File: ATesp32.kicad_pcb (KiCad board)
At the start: 4 copper layers, 18 x 51.2 mm, 51 parts, among them J1 USB_C_Receptacle_USB2.0_16P, J2 JST PH, Q1 DMP2045U, SW1 RESET, SW2 BOOT, U1 ESP32-S3, U2 ATmega32A-P, U3 MCP73831-2-OT, U4 AP2112K-3.3, U5 CP2102N-Axx-xQFN24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

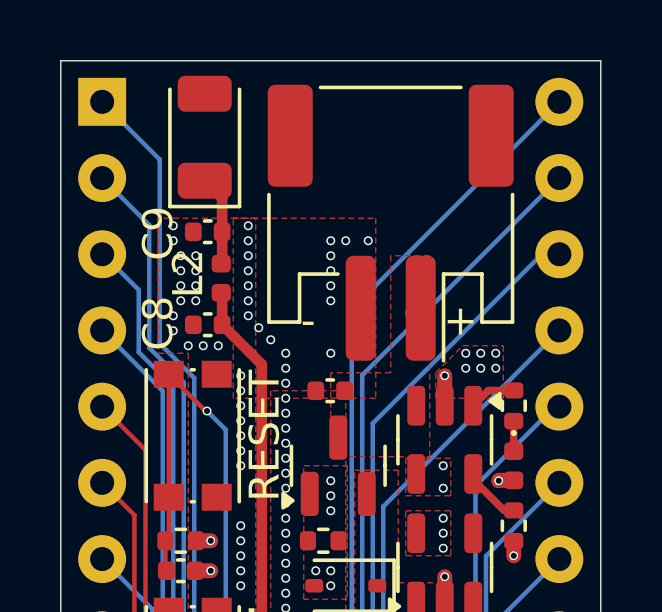
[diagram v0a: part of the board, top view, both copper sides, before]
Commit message: fix bug - correct use of open drain status signal of lipo charger
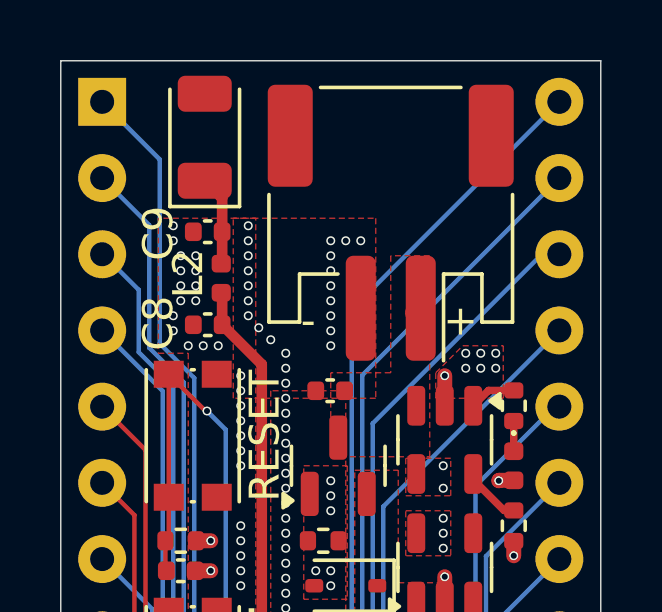
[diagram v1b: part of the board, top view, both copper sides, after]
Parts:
- U3: value MCP73831-2-OT -> MCP73832
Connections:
- D2 pad 2: GND -> +5V
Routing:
- net +5V: track 0.00 -> 0.51 mm, vias 17 -> 18
- net GND: track 11.4 -> 10.9 mm, vias 113 -> 114
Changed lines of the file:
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@@
 			)
 		)
-		(property "Value" "MCP73831-2-OT"
+		(property "Value" "MCP73832"
 			(at 0 2.4 90)
 			(layer "F.Fab")
@@
 			(layers "F.Cu" "F.Paste" "F.Mask")
 			(roundrect_rratio 0.25)
-			(net 3 "GND")
+			(net 6 "+5V")
 			(pinfunction "A")
 			(pintype "passive")
@@
 	)
 	(segment
-		(start 90.1 63.985)
-		(end 89.615 63.985)
-		(width 0.5)
-		(layer "F.Cu")
-		(net 3)
-	)
-	(segment
 		(start 87.8 61.5)
 		(end 87.8 60.5)
@@
 	)
 	(segment
-		(start 89.615 63.985)
-		(end 89.6 64)
-		(width 0.5)
-		(layer "F.Cu")
-		(net 3)
-	)
-	(segment
 		(start 83.25 92.732108)
 		(end 83.259699 92.741807)
@@
 	)
 	(via
+		(at 84 58.5)
+		(size 0.3)
+		(drill 0.2)
+		(layers "F.Cu" "B.Cu")
+		(free yes)
+		(net 3)
+	)
+	(via
 		(at 87.5 87.85)
 		(size 0.3)
@@
 	)
 	(via
-		(at 84 59.75)
+		(at 84 59.5)
 		(size 0.3)
 		(drill 0.2)
@@
 	)
 	(via
+		(at 84 59)
+		(size 0.3)
+		(drill 0.2)
+		(layers "F.Cu" "B.Cu")
+		(free yes)
+		(net 3)
+	)
+	(via
 		(at 81.25 58.5)
 		(size 0.3)
@@
 	)
 	(via
-		(at 89.6 64)
-		(size 0.3)
-		(drill 0.2)
-		(layers "F.Cu" "B.Cu")
-		(net 3)
-	)
-	(via
 		(at 82.5 66.75)
 		(size 0.3)
@@
 	)
 	(via
-		(at 85.25 56)
+		(at 85 56)
 		(size 0.3)
 		(drill 0.2)
@@
 		(net 5)
 	)
+	(segment
+		(start 90.1 63.985)
+		(end 89.615 63.985)
+		(width 0.5)
+		(layer "F.Cu")
+		(net 6)
+	)
+	(segment
+		(start 89.615 63.985)
+		(end 89.6 64)
+		(width 0.5)
+		(layer "F.Cu")
+		(net 6)
+	)
 	(via
 		(at 84 67)
@@
 		(net 6)
 	)
+	(via
+		(at 89.6 64)
+		(size 0.3)
+		(drill 0.2)
+		(layers "F.Cu" "B.Cu")
+		(net 6)
+	)

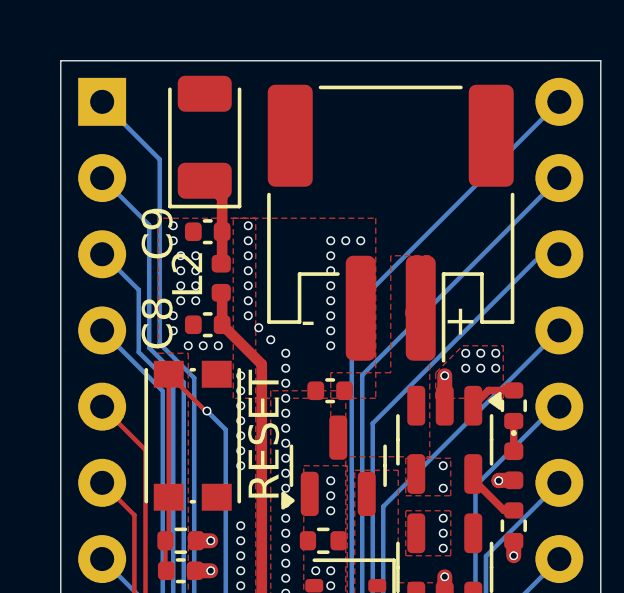
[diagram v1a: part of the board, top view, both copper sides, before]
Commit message: spec components for JLC
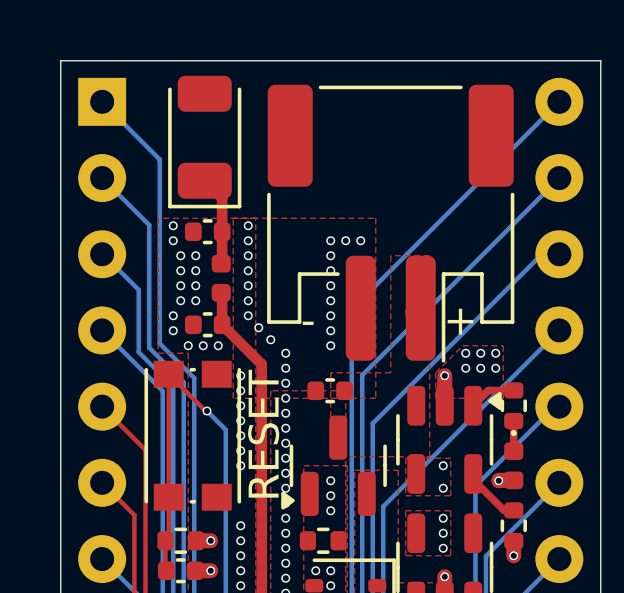
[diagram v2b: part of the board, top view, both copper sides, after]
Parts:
- R14, R15, R6: value 10K -> 5.1K
- U2: value ATmega32A-P -> HEADER

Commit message: Generate production files. More clear part names for ESP and LiPo charger
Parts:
- U1: value ESP32-S3 -> ESP32-S3FH4R2
- U3: value MCP73832 -> MCP73832-2
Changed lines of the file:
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@@
 			(viasonmask no)
 			(mode 1)
-			(useauxorigin no)
+			(useauxorigin yes)
 			(hpglpennumber 1)
 			(hpglpenspeed 20)
@@
 			(outputformat 1)
 			(mirror no)
-			(drillshape 1)
+			(drillshape 0)
 			(scaleselection 1)
-			(outputdirectory "")
+			(outputdirectory "Fabrication/")
 		)
 	)
@@
 			)
 		)
-		(property "Value" "MCP73832"
+		(property "Value" "MCP73832-2"
 			(at 0 2.4 90)
 			(layer "F.Fab")
@@
 		(sheetname "Root")
 		(sheetfile "ATesp32.kicad_sch")
-		(attr through_hole exclude_from_pos_files allow_missing_courtyard)
+		(attr through_hole exclude_from_pos_files exclude_from_bom allow_missing_courtyard
+			dnp
+		)
 		(fp_line
 			(start 0.255 -0.27)
@@
 			)
 		)
-		(property "Value" "ESP32-S3"
+		(property "Value" "ESP32-S3FH4R2"
 			(at 0 4.800001 135)
 			(layer "F.Fab")
@@
 		(tags "capacitor")
 		(property "Reference" "C8"
-			(at 1.65 0.05 270)
+			(at 1.65 0.05 -90)
 			(layer "F.SilkS")
 			(hide yes)
@@
 		(sheetfile "ATesp32.kicad_sch")
 		(zone_connect 1)
-		(attr exclude_from_pos_files exclude_from_bom)
+		(attr exclude_from_pos_files exclude_from_bom dnp)
 		(fp_line
 			(start -0.7 -1)
@@
 		(sheetfile "ATesp32.kicad_sch")
 		(zone_connect 1)
-		(attr exclude_from_pos_files exclude_from_bom)
+		(attr exclude_from_pos_files exclude_from_bom dnp)
 		(fp_line
 			(start 1.4 -0.3)
@@
 		(sheetfile "ATesp32_USB.kicad_sch")
 		(zone_connect 1)
-		(attr exclude_from_pos_files exclude_from_bom)
+		(attr exclude_from_pos_files exclude_from_bom dnp)
 		(net_tie_pad_groups "1, 2")
 		(fp_poly
@@
 		(sheetfile "ATesp32_USB.kicad_sch")
 		(zone_connect 1)
-		(attr exclude_from_pos_files exclude_from_bom)
+		(attr exclude_from_pos_files exclude_from_bom dnp)
 		(net_tie_pad_groups "1, 2")
 		(fp_poly

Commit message: Add some Mouser PNs
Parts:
- J1: footprint Connector_USB:USB_C_Receptacle_G-Switch_GT-USB-7010ASV -> Connector_USB:USB_C_Receptacle_GCT_USB4105-xx-A_16P_TopMnt_Horizontal

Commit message: update manf outputs
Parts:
- U3: value MCP73832-2 -> MCP73832T-2
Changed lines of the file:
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@@
 			)
 		)
-		(property "Mouser" "187-CL05B104KO5NNNC"
+		(property "Mouser" ""
 			(at 0 0 45)
 			(unlocked yes)
@@
 			)
 		)
-		(property "Mouser" "187-CL05B104KO5NNNC"
+		(property "Mouser" ""
 			(at 0 0 -135)
 			(unlocked yes)
@@
 			)
 		)
+		(property "DigiKey" "AP2112K-3.3TRG1DICT-ND"
+			(at 0 0 90)
+			(unlocked yes)
+			(layer "F.Fab")
+			(hide yes)
+			(effects
+				(font
+					(size 1 1)
+					(thickness 0.15)
+				)
+			)
+		)
 		(property ki_fp_filters "SOT?23?5*")
 		(sheetname "POWER")
@@
 			)
 		)
-		(property "Value" "MCP73832-2"
+		(property "Value" "MCP73832T-2"
 			(at 0 2.4 90)
 			(layer "F.Fab")
@@
 			)
 		)
+		(property "DigiKey" "MCP73832T-2ACI/OTCT-ND"
+			(at 0 0 -90)
+			(unlocked yes)
+			(layer "F.Fab")
+			(hide yes)
+			(effects
+				(font
+					(size 1 1)
+					(thickness 0.15)
+				)
+			)
+		)
 		(property ki_fp_filters "SOT?23*")
 		(sheetname "POWER")
@@
 			)
 		)
-		(property "Mouser" "187-CL05B104KO5NNNC"
+		(property "Mouser" ""
 			(at 0 0 135)
 			(unlocked yes)
@@
 			)
 		)
+		(property "DigiKey" "336-5887-ND"
+			(at 0 0 90)
+			(unlocked yes)
+			(layer "F.Fab")
+			(hide yes)
+			(effects
+				(font
+					(size 1 1)
+					(thickness 0.15)
+				)
+			)
+		)
 		(property ki_fp_filters "QFN*4x4mm*P0.5mm*")
 		(sheetname "USB")
@@
 			)
 		)
-		(property "Mouser" "187-CL05B104KO5NNNC"
+		(property "Mouser" ""
 			(at 0 0 0)
 			(unlocked yes)
@@
 			)
 		)
-		(property "Mouser" "187-CL05B104KO5NNNC"
+		(property "Mouser" ""
 			(at 0 0 -135)
 			(unlocked yes)
@@
 			)
 		)
-		(property "Mouser" "187-CL05B104KO5NNNC"
+		(property "Mouser" ""
 			(at 0 0 -90)
 			(unlocked yes)

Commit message: USB-UART Bridge LEDs had wrong orientation. Fixed
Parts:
- turned D5 to 180 degrees
- turned D6 to 180 degrees
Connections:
- D5 pad 1: Net-(D5-K) -> GND
- D5 pad 2: GND -> Net-(D5-A)
- D6 pad 1: Net-(D6-K) -> GND
- D6 pad 2: GND -> Net-(D6-A)
- R14 pad 2: Net-(D5-K) -> Net-(D5-A)
- R15 pad 2: Net-(D6-K) -> Net-(D6-A)
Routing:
- net Net-(D5-K): track 1.51 -> 0.00 mm
- net Net-(D5-A): track 0.00 -> 1.51 mm
- net Net-(D6-K): track 1.01 -> 0.00 mm
- net Net-(D6-A): track 0.00 -> 1.01 mm
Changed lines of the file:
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@@
 	(net 11 "Net-(U5-VDD)")
 	(net 12 "Net-(D2-K)")
-	(net 13 "Net-(D5-K)")
-	(net 14 "Net-(D6-K)")
+	(net 13 "Net-(D5-A)")
+	(net 14 "Net-(D6-A)")
 	(net 15 "Net-(J1-CC2)")
 	(net 16 "D-")
@@
 			(layers "F.Cu" "F.Paste" "F.Mask")
 			(roundrect_rratio 0.25)
-			(net 13 "Net-(D5-K)")
+			(net 13 "Net-(D5-A)")
 			(pintype "passive")
 		)
@@
 	(footprint "LED_SMD:LED_0402_1005Metric"
 		(layer "F.Cu")
-		(at 87.9 87)
+		(at 87.9 87 180)
 		(descr "LED SMD 0402 (1005 Metric), square (rectangular) end terminal, IPC_7351 nominal, (Body size source: http://www.tortai-tech.com/upload/download/2011102023233369053.pdf), generated with kicad-footprint-generator")
 		(tags "LED")
 		(property "Reference" "D6"
-			(at 0 -1.17 0)
+			(at 0 -1.17 360)
 			(layer "F.SilkS")
 			(hide yes)
@@
 		)
 		(property "Value" "LED_Small"
-			(at 0 1.17 0)
+			(at 0 1.17 360)
 			(layer "F.Fab")
 			(effects
@@
 		)
 		(property "Footprint" "LED_SMD:LED_0402_1005Metric"
-			(at 0 0 0)
+			(at 0 0 180)
 			(unlocked yes)
 			(layer "F.Fab")
@@
 		)
 		(property "Datasheet" ""
-			(at 0 0 0)
+			(at 0 0 180)
 			(unlocked yes)
 			(layer "F.Fab")
@@
 		)
 		(property "Description" "Light emitting diode, small symbol"
-			(at 0 0 0)
+			(at 0 0 180)
 			(unlocked yes)
 			(layer "F.Fab")
@@
 		)
 		(property "Sim.Device" ""
-			(at 0 0 0)
+			(at 0 0 180)
 			(unlocked yes)
 			(layer "F.Fab")
@@
 		)
 		(property "Sim.Pins" ""
-			(at 0 0 0)
+			(at 0 0 180)
 			(unlocked yes)
 			(layer "F.Fab")
@@
 		)
 		(property "Sim.Type" ""
-			(at 0 0 0)
+			(at 0 0 180)
 			(unlocked yes)
 			(layer "F.Fab")
@@
 		)
 		(property "LCSC" "C510300"
-			(at 0 0 0)
+			(at 0 0 180)
 			(unlocked yes)
 			(layer "F.Fab")
@@
 		)
 		(property "DigiKey" "SML-P11UTT86RCT-ND"
-			(at 0 0 0)
+			(at 0 0 180)
 			(unlocked yes)
 			(layer "F.Fab")
@@
 		)
 		(fp_line
-			(start -0.93 -0.47)
-			(end 0.93 -0.47)
+			(start 0.93 0.47)
+			(end -0.93 0.47)
 			(stroke
 				(width 0.05)
@@
 		)
 		(fp_line
-			(start -0.93 0.47)
-			(end -0.93 -0.47)
+			(start 0.93 -0.47)
+			(end 0.93 0.47)
 			(stroke
 				(width 0.05)
@@
 		)
 		(fp_line
-			(start 0.93 -0.47)
-			(end 0.93 0.47)
+			(start -0.93 0.47)
+			(end -0.93 -0.47)
 			(stroke
 				(width 0.05)
@@
 		)
 		(fp_line
-			(start 0.93 0.47)
-			(end -0.93 0.47)
+			(start -0.93 -0.47)
+			(end 0.93 -0.47)
 			(stroke
 				(width 0.05)
@@
 		)
 		(fp_line
-			(start -0.5 -0.25)
-			(end 0.5 -0.25)
+			(start 0.5 0.25)
+			(end -0.5 0.25)
 			(stroke
 				(width 0.1)
@@
 		)
 		(fp_line
-			(start -0.5 0.25)
-			(end -0.5 -0.25)
+			(start 0.5 -0.25)
+			(end 0.5 0.25)
 			(stroke
 				(width 0.1)
@@
 		)
 		(fp_line
-			(start -0.4 0.25)
-			(end -0.4 -0.25)
+			(start -0.3 0.25)
+			(end -0.3 -0.25)
 			(stroke
 				(width 0.1)
@@
 		)
 		(fp_line
-			(start -0.3 0.25)
-			(end -0.3 -0.25)
+			(start -0.4 0.25)
+			(end -0.4 -0.25)
 			(stroke
 				(width 0.1)
@@
 		)
 		(fp_line
-			(start 0.5 -0.25)
-			(end 0.5 0.25)
+			(start -0.5 0.25)
+			(end -0.5 -0.25)
 			(stroke
 				(width 0.1)
@@
 		)
 		(fp_line
-			(start 0.5 0.25)
-			(end -0.5 0.25)
+			(start -0.5 -0.25)
+			(end 0.5 -0.25)
 			(stroke
 				(width 0.1)
@@
 		)
 		(fp_text user "${REFERENCE}"
-			(at 0 0 0)
+			(at 0 0 360)
 			(layer "F.Fab")
 			(effects
@@
 		)
 		(pad "1" smd roundrect
-			(at -0.485 0)
+			(at -0.485 0 180)
 			(size 0.59 0.64)
 			(layers "F.Cu" "F.Paste" "F.Mask")
 			(roundrect_rratio 0.25)
-			(net 14 "Net-(D6-K)")
+			(net 3 "GND")
 			(pinfunction "K")
 			(pintype "passive")
 		)
 		(pad "2" smd roundrect
-			(at 0.485 0)
+			(at 0.485 0 180)
 			(size 0.59 0.64)
 			(layers "F.Cu" "F.Paste" "F.Mask")
 			(roundrect_rratio 0.25)
-			(net 3 "GND")
+			(net 14 "Net-(D6-A)")
 			(pinfunction "A")
 			(pintype "passive")
@@
 	(footprint "LED_SMD:LED_0402_1005Metric"
 		(layer "F.Cu")
-		(at 87.9 86)
+		(at 87.9 86 180)
 		(descr "LED SMD 0402 (1005 Metric), square (rectangular) end terminal, IPC_7351 nominal, (Body size source: http://www.tortai-tech.com/upload/download/2011102023233369053.pdf), generated with kicad-footprint-generator")
 		(tags "LED")
 		(property "Reference" "D5"
-			(at 0 -1.17 0)
+			(at 0 -1.17 360)
 			(layer "F.SilkS")
 			(hide yes)
@@
 		)
 		(property "Value" "LED_Small"
-			(at 0 1.17 0)
+			(at 0 1.17 360)
 			(layer "F.Fab")
 			(effects
@@
 		)
 		(property "Footprint" "LED_SMD:LED_0402_1005Metric"
-			(at 0 0 0)
+			(at 0 0 180)
 			(unlocked yes)
 			(layer "F.Fab")
@@
 		)
 		(property "Datasheet" ""
-			(at 0 0 0)
+			(at 0 0 180)
 			(unlocked yes)
 			(layer "F.Fab")
@@
 		)
 		(property "Description" "Light emitting diode, small symbol"
-			(at 0 0 0)
+			(at 0 0 180)
 			(unlocked yes)
 			(layer "F.Fab")
@@
 		)
 		(property "Sim.Device" ""
-			(at 0 0 0)
+			(at 0 0 180)
 			(unlocked yes)
 			(layer "F.Fab")
@@
 		)
 		(property "Sim.Pins" ""
-			(at 0 0 0)
+			(at 0 0 180)
 			(unlocked yes)
 			(layer "F.Fab")
@@
 		)
 		(property "Sim.Type" ""
-			(at 0 0 0)
+			(at 0 0 180)
 			(unlocked yes)
 			(layer "F.Fab")
@@
 		)
 		(property "LCSC" "C510300"
-			(at 0 0 0)
+			(at 0 0 180)
 			(unlocked yes)
 			(layer "F.Fab")
@@
 		)
 		(property "DigiKey" "SML-P11UTT86RCT-ND"
-			(at 0 0 0)
+			(at 0 0 180)
 			(unlocked yes)
 			(layer "F.Fab")
@@
 		)
 		(fp_line
-			(start -0.93 -0.47)
-			(end 0.93 -0.47)
+			(start 0.93 0.47)
+			(end -0.93 0.47)
 			(stroke
 				(width 0.05)
@@
 		)
 		(fp_line
-			(start -0.93 0.47)
-			(end -0.93 -0.47)
+			(start 0.93 -0.47)
+			(end 0.93 0.47)
 			(stroke
 				(width 0.05)
@@
 		)
 		(fp_line
-			(start 0.93 -0.47)
-			(end 0.93 0.47)
+			(start -0.93 0.47)
+			(end -0.93 -0.47)
 			(stroke
 				(width 0.05)
@@
 		)
 		(fp_line
-			(start 0.93 0.47)
-			(end -0.93 0.47)
+			(start -0.93 -0.47)
+			(end 0.93 -0.47)
 			(stroke
 				(width 0.05)
@@
 		)
 		(fp_line
-			(start -0.5 -0.25)
-			(end 0.5 -0.25)
+			(start 0.5 0.25)
+			(end -0.5 0.25)
 			(stroke
 				(width 0.1)
@@
 		)
 		(fp_line
-			(start -0.5 0.25)
-			(end -0.5 -0.25)
+			(start 0.5 -0.25)
+			(end 0.5 0.25)
 			(stroke
 				(width 0.1)
@@
 		)
 		(fp_line
-			(start -0.4 0.25)
-			(end -0.4 -0.25)
+			(start -0.3 0.25)
+			(end -0.3 -0.25)
 			(stroke
 				(width 0.1)
@@
 		)
 		(fp_line
-			(start -0.3 0.25)
-			(end -0.3 -0.25)
+			(start -0.4 0.25)
+			(end -0.4 -0.25)
 			(stroke
 				(width 0.1)
@@
 		)
 		(fp_line
-			(start 0.5 -0.25)
-			(end 0.5 0.25)
+			(start -0.5 0.25)
+			(end -0.5 -0.25)
 			(stroke
 				(width 0.1)
@@
 		)
 		(fp_line
-			(start 0.5 0.25)
-			(end -0.5 0.25)
+			(start -0.5 -0.25)
+			(end 0.5 -0.25)
 			(stroke
 				(width 0.1)
@@
 		)
 		(fp_text user "${REFERENCE}"
-			(at 0 0 0)
+			(at 0 0 360)
 			(layer "F.Fab")
 			(effects
@@
 		)
 		(pad "1" smd roundrect
-			(at -0.485 0)
+			(at -0.485 0 180)
 			(size 0.59 0.64)
 			(layers "F.Cu" "F.Paste" "F.Mask")
 			(roundrect_rratio 0.25)
-			(net 13 "Net-(D5-K)")
+			(net 3 "GND")
 			(pinfunction "K")
 			(pintype "passive")
 		)
 		(pad "2" smd roundrect
-			(at 0.485 0)
+			(at 0.485 0 180)
 			(size 0.59 0.64)
 			(layers "F.Cu" "F.Paste" "F.Mask")
 			(roundrect_rratio 0.25)
-			(net 3 "GND")
+			(net 13 "Net-(D5-A)")
 			(pinfunction "A")
 			(pintype "passive")
@@
 			(layers "F.Cu" "F.Paste" "F.Mask")
 			(roundrect_rratio 0.25)
-			(net 14 "Net-(D6-K)")
+			(net 14 "Net-(D6-A)")
 			(pintype "passive")
 		)
@@
 		(polygon
 			(pts
-				(xy 88 85.65) (xy 88.85 85.65) (xy 88.85 88.55) (xy 88 88.55) (xy 88 88.1) (xy 86.7 88.1) (xy 86.7 87.5)
+				(xy 87.95 85.65) (xy 88.85 85.65) (xy 88.85 88.55) (xy 88 88.55) (xy 88 88.1) (xy 86.7 88.1) (xy 86.7 87.5)
 				(xy 87.95 87.5)
 			)

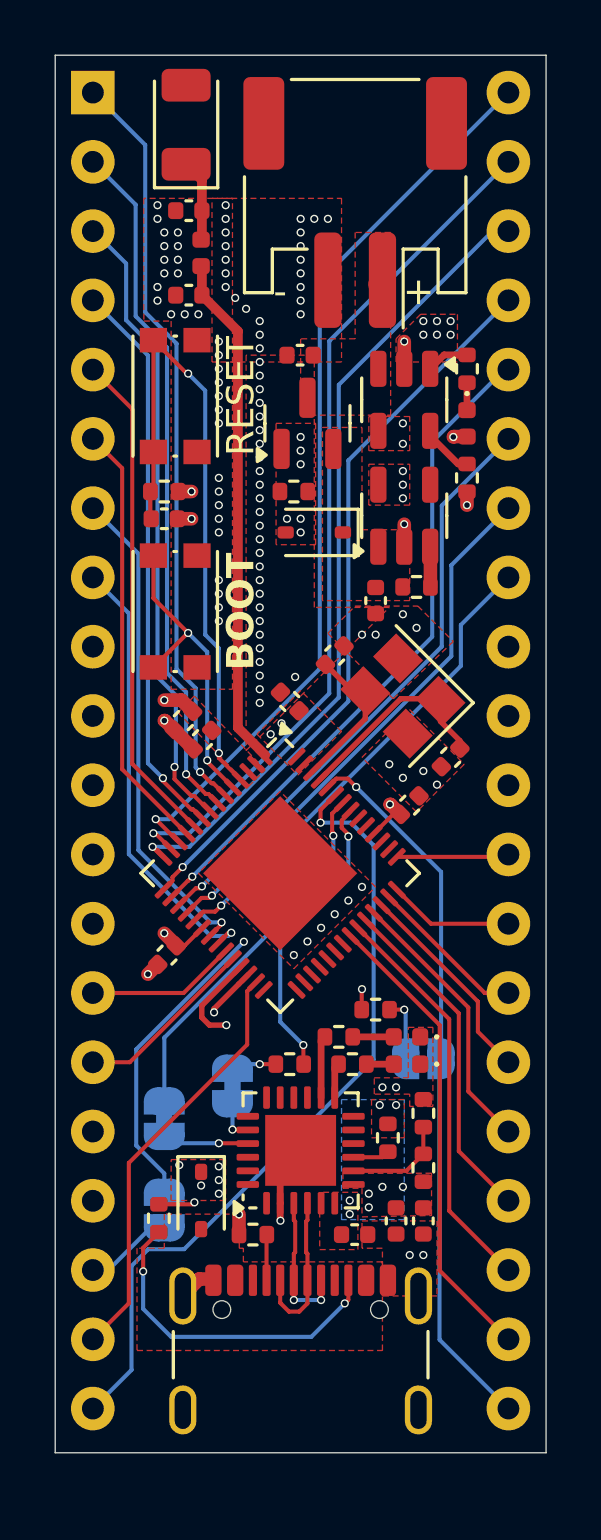
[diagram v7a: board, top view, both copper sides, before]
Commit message: LEDs were persistently on. Change to active low config see CP2102N datasheet fig 4.3
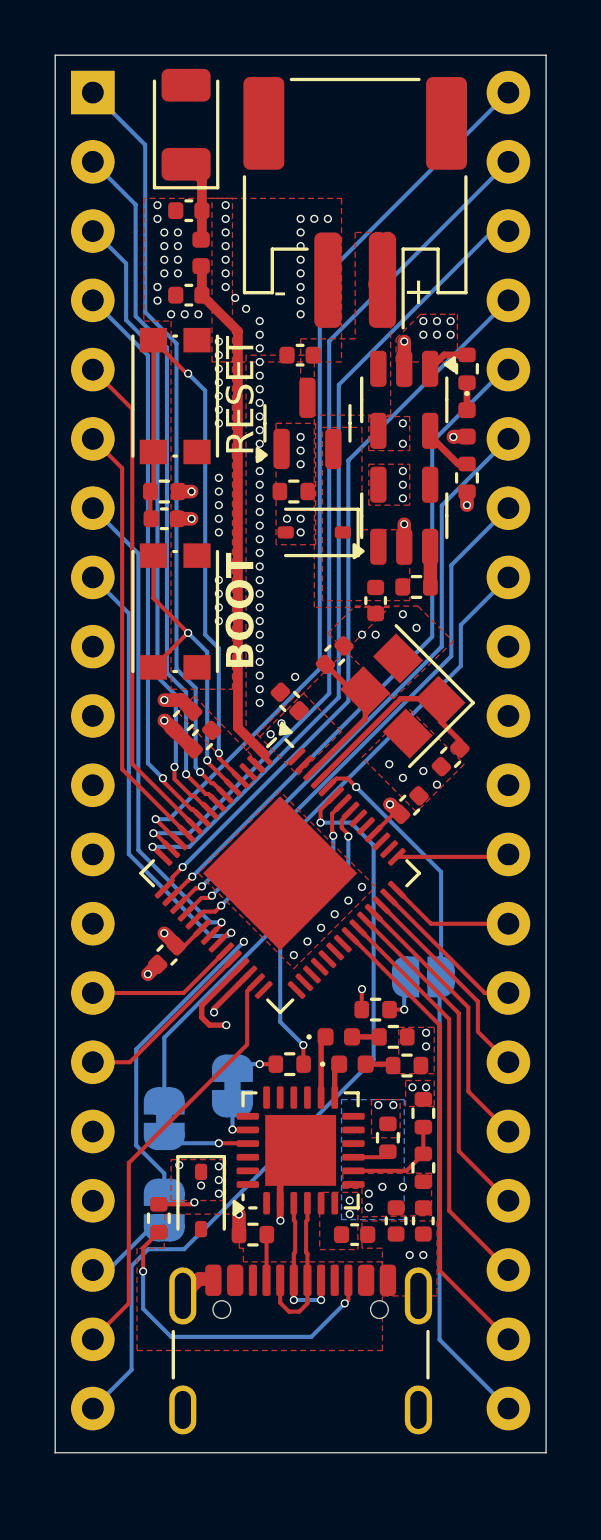
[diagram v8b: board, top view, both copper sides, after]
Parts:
- moved JP6 3.00 mm to (88.5, 83.8)
- moved D5 2.50 mm to (85.4, 86.0), turned to 0 degrees
- moved R15 2.00 mm to (87.9, 87.0)
- moved D6 2.00 mm to (85.9, 87.0), turned to 0 degrees
- moved R14 2.00 mm to (87.4, 86.0)
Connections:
- D5 pad 1: GND -> Net-(D5-K)
- D6 pad 1: GND -> Net-(D6-K)
- R14 pad 1: Net-(U5-~{TXT}/GPIO.0) -> Net-(D5-A)
- R14 pad 2: Net-(D5-A) -> +5V
- R15 pad 1: Net-(U5-~{RXT}/GPIO.1) -> Net-(D6-A)
- R15 pad 2: Net-(D6-A) -> +5V
- U5 pad 13: Net-(U5-~{RXT}/GPIO.1) -> Net-(D6-K)
- U5 pad 14: Net-(U5-~{TXT}/GPIO.0) -> Net-(D5-K)
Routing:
- net Net-(D5-K): track 0.00 -> 2.29 mm
- net Net-(U5-~{TXT}/GPIO.0): track 2.08 -> 0.00 mm
- net Net-(D6-K): track 0.00 -> 1.29 mm
- net Net-(U5-~{RXT}/GPIO.1): track 1.08 -> 0.00 mm
- net PD7: track 25.9 -> 26.5 mm
- net Net-(JP6-B): track 2.36 -> 1.76 mm
- net Net-(D5-A): track 1.51 -> 1.00 mm
- net +5V: vias 18 -> 20
